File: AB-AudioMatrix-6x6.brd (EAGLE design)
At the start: 188 x 72 mm, 53 parts, among them IC10 TL072D, IC11 TL072D, IC12 TL072D, IC13 TL072D, IC14 TL072D, IC9 TL072D

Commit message: Platine grundlegend fertiggestellt
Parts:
- removed U$13: (no value), frames:A4L-LOC
- moved J1 3.00 mm to (66.0, 46.0)
- moved J2 3.00 mm to (161.0, 46.0)
- moved J3 3.00 mm to (66.0, 38.0)
- moved J4 3.00 mm to (161.0, 38.0)
- moved R1 3.00 mm to (10.0, 64.0)
- moved R10 3.00 mm to (66.0, 64.0)
- moved R11 3.00 mm to (86.0, 64.0)
- moved R12 3.00 mm to (80.0, 64.0)
- moved R13 3.00 mm to (111.0, 64.0)
- moved R14 3.00 mm to (105.0, 64.0)
- moved R15 3.00 mm to (125.0, 64.0)
- moved R16 3.00 mm to (119.0, 64.0)
- moved R17 3.00 mm to (139.0, 64.0)
- moved R18 3.00 mm to (133.0, 64.0)
- moved R19 3.00 mm to (153.0, 64.0)
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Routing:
- net OUT2L: track 47.4 -> 239.4 mm, vias 0 -> 4
- net N$69: track 154.4 -> 6.78 mm, vias 1 -> 0
- net IN1L: track 198.4 -> 329.8 mm
- net GND: track 0.00 -> 104.8 mm, vias 0 -> 48
- net IN2L: track 190.7 -> 294.4 mm, vias 0 -> 2
- net IN1R: track 171.1 -> 268.0 mm
- net IN3L: track 187.4 -> 279.5 mm, vias 0 -> 2
- net IN6L: track 167.4 -> 246.3 mm, vias 1 -> 2
- net IN3R: track 178.1 -> 253.8 mm, vias 1 -> 3
- net IN6R: track 205.1 -> 280.8 mm, vias 0 -> 1
- net IN2R: track 173.6 -> 249.1 mm, vias 1 -> 3
- net IN4L: track 177.6 -> 246.8 mm, vias 1 -> 2
- net OUT6R: track 69.4 -> 135.6 mm, vias 0 -> 1
- net OUT6L: track 55.9 -> 118.6 mm, vias 0 -> 1
- net IN5L: track 170.4 -> 230.2 mm, vias 1 -> 2
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- added copper zone on layer 2, net +12V
- added copper zone on layer 16, net -12V
- added copper zone on layer 3, net GND
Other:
- board size 188 x 72 mm -> 188 x 69 mm

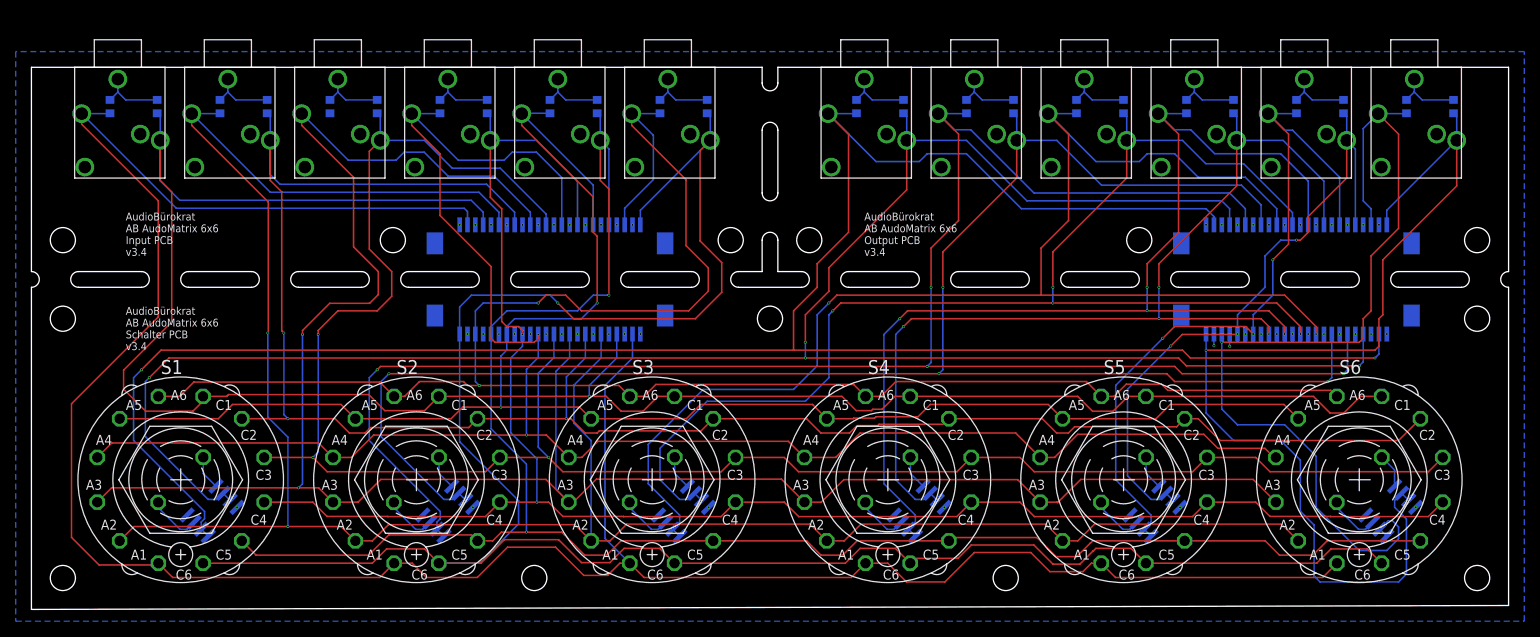
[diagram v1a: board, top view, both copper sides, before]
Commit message: 3,5 mm Klinken Buchsen ausgetauscht | Spannungsversorgung hinzugefügt | Fusion 3D-Modell vollständig
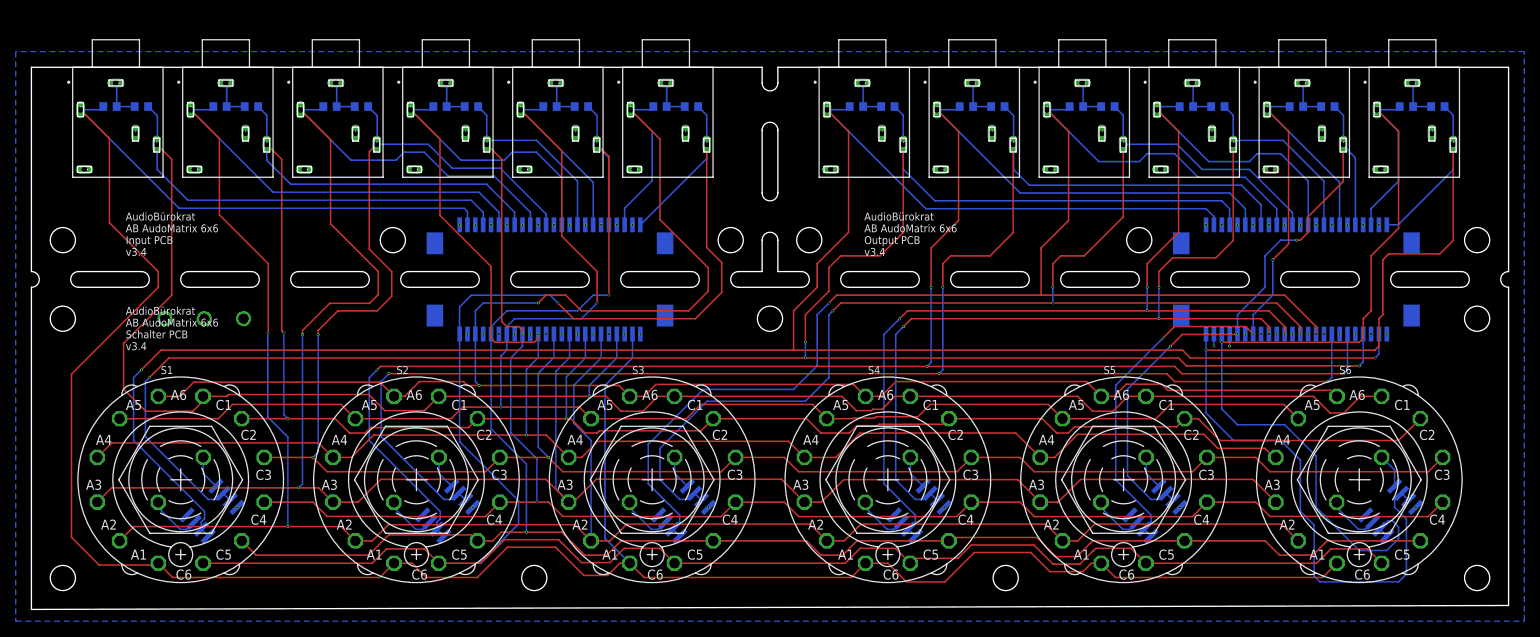
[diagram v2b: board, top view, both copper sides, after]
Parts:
- removed U$1, U$10, U$11, U$12, U$2, U$3, U$4, U$5, U$6, U$7, U$8, U$9: KLINKE3,5, Mario - Klinke Stecker 3,5:KLINKE3,5
- added J8: (no value), Wurth_Connectors_WR-TBL Wire Protector:691102710003
- added X1, X10, X11, X12, X2, X3, X4, X5, X6, X7, X8, X9: 35RAPC4BH3-2, h8-conector:SWITCHCRAFT_35RAPC4BH3
- moved R11 2.00 mm to (84.0, 64.0), turned to 180 degrees
- moved R13 2.00 mm to (109.0, 64.0), turned to 180 degrees
- moved R15 2.00 mm to (123.0, 64.0), turned to 180 degrees
- moved R17 2.00 mm to (137.0, 64.0), turned to 180 degrees
- moved R19 2.00 mm to (151.0, 64.0), turned to 180 degrees
- moved R2 2.00 mm to (28.0, 64.0), turned to 180 degrees
- moved R21 2.00 mm to (165.0, 64.0), turned to 180 degrees
- moved R23 2.00 mm to (179.0, 64.0), turned to 180 degrees
- moved R4 2.00 mm to (42.0, 64.0), turned to 180 degrees
- moved R6 2.00 mm to (14.0, 64.0), turned to 180 degrees
- moved R7 2.00 mm to (56.0, 64.0), turned to 180 degrees
- moved R9 2.00 mm to (70.0, 64.0), turned to 180 degrees
- turned R1 to 0 degrees
- turned R10 to 0 degrees
- turned R12 to 0 degrees
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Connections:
- net +12V: now also J8.1
- net -12V: now also J8.3
- net GND: now also J8.2, X1.1, X1.3, X1.4, X10.1, X10.3, X10.4, X11.1, X11.3, X11.4, X12.1, X12.3, X12.4, X2.1, X2.3, X2.4, X3.1, X3.3, X3.4, X4.1, X4.3, X4.4, X5.1, X5.3, X5.4, X6.1, X6.3, X6.4, X7.1, X7.3, X7.4, X8.1, X8.3, X8.4, X9.1, X9.3, X9.4; no longer U$1.GND, U$1.LEFT_OFF, U$1.RIGHT_OFF, U$10.GND, U$10.LEFT_OFF, U$10.RIGHT_OFF, U$11.GND, U$11.LEFT_OFF, U$11.RIGHT_OFF, U$12.GND, U$12.LEFT_OFF, U$12.RIGHT_OFF, U$2.GND, U$2.LEFT_OFF, U$2.RIGHT_OFF, U$3.GND, U$3.LEFT_OFF, U$3.RIGHT_OFF, U$4.GND, U$4.LEFT_OFF, U$4.RIGHT_OFF, U$5.GND, U$5.LEFT_OFF, U$5.RIGHT_OFF, U$6.GND, U$6.LEFT_OFF, U$6.RIGHT_OFF, U$7.GND, U$7.LEFT_OFF, U$7.RIGHT_OFF, U$8.GND, U$8.LEFT_OFF, U$8.RIGHT_OFF, U$9.GND, U$9.LEFT_OFF, U$9.RIGHT_OFF
- net IN1L: now also X1.5; no longer U$1.LEFT
- net IN1R: now also X1.2; no longer U$1.RIGHT
- net IN2L: now also X2.5; no longer U$2.LEFT
- net IN2R: now also X2.2; no longer U$2.RIGHT
- net IN3L: now also X3.5; no longer U$3.LEFT
- net IN3R: now also X3.2; no longer U$3.RIGHT
- net IN4L: now also X4.5; no longer U$4.LEFT
- net IN4R: now also X4.2; no longer U$4.RIGHT
- net IN5L: now also X5.5; no longer U$5.LEFT
- net IN5R: now also X5.2; no longer U$5.RIGHT
- net IN6L: now also X6.5; no longer U$6.LEFT
- net IN6R: now also X6.2; no longer U$6.RIGHT
- net OUT1L: now also X7.5; no longer U$7.LEFT
- net OUT1R: now also X7.2; no longer U$7.RIGHT
- net OUT2L: now also X8.5; no longer U$8.LEFT
- net OUT2R: now also X8.2; no longer U$8.RIGHT
- net OUT3L: now also X9.5; no longer U$9.LEFT
- net OUT3R: now also X9.2; no longer U$9.RIGHT
- net OUT4L: now also X10.5; no longer U$10.LEFT
- net OUT4R: now also X10.2; no longer U$10.RIGHT
- net OUT5L: now also X11.5; no longer U$11.LEFT
- net OUT5R: now also X11.2; no longer U$11.RIGHT
- net OUT6L: now also X12.5; no longer U$12.LEFT
- net OUT6R: now also X12.2; no longer U$12.RIGHT
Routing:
- net GND: track 104.8 -> 67.1 mm
- net OUT2R: track 223.8 -> 229.9 mm
- net OUT1R: track 265.6 -> 271.6 mm
- net OUT6R: track 135.6 -> 140.6 mm
- net OUT4R: track 124.4 -> 129.3 mm
- net IN3L: track 279.5 -> 283.5 mm
- net OUT3R: track 161.7 -> 164.7 mm
- net IN4R: track 230.7 -> 232.7 mm
- net OUT6L: track 118.6 -> 120.4 mm
- net IN5R: track 239.2 -> 240.5 mm
- net IN3R: track 253.8 -> 255.0 mm
- net OUT4L: track 141.8 -> 143.0 mm
- net OUT5R: track 82.4 -> 83.2 mm
- net IN5L: track 230.2 -> 230.7 mm
- net IN1R: track 268.0 -> 268.6 mm
